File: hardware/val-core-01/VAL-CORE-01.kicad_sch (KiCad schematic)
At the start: 15 parts, among them J1 USB-C Device/UFP, J2 TRS MIDI OUT Type-A, J3 TRS MIDI IN Type-A, U1 ESP32-S3-MINI-1-N4R2, U2 TUSB320LAI, U3 3V3_REGULATOR_TBD_600mA, U4 SN74AHCT1G125, U5 MIDI_IN_OPTO_TBD

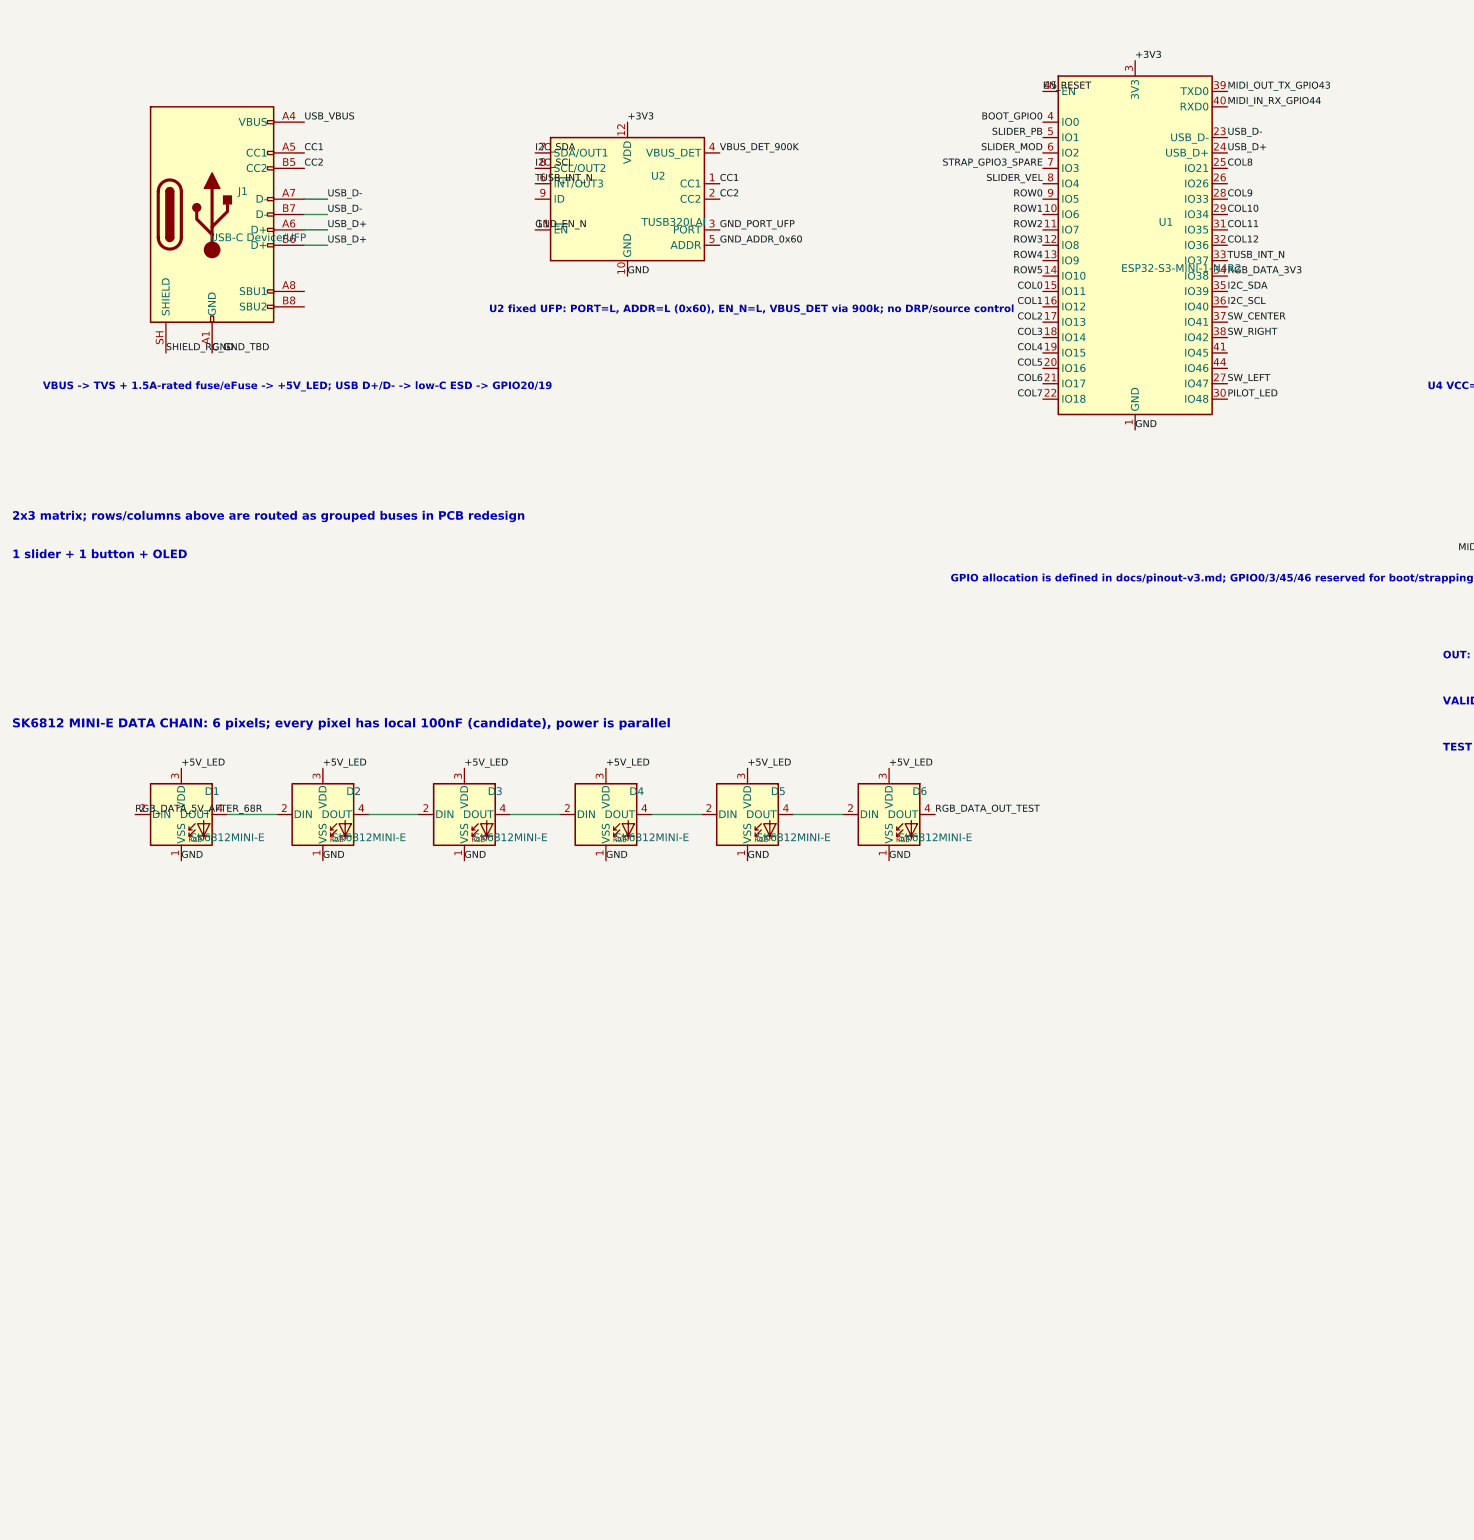
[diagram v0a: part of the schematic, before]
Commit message: VAL-CORE-01の旧CC回路と検証条件を現行仕様へ修正
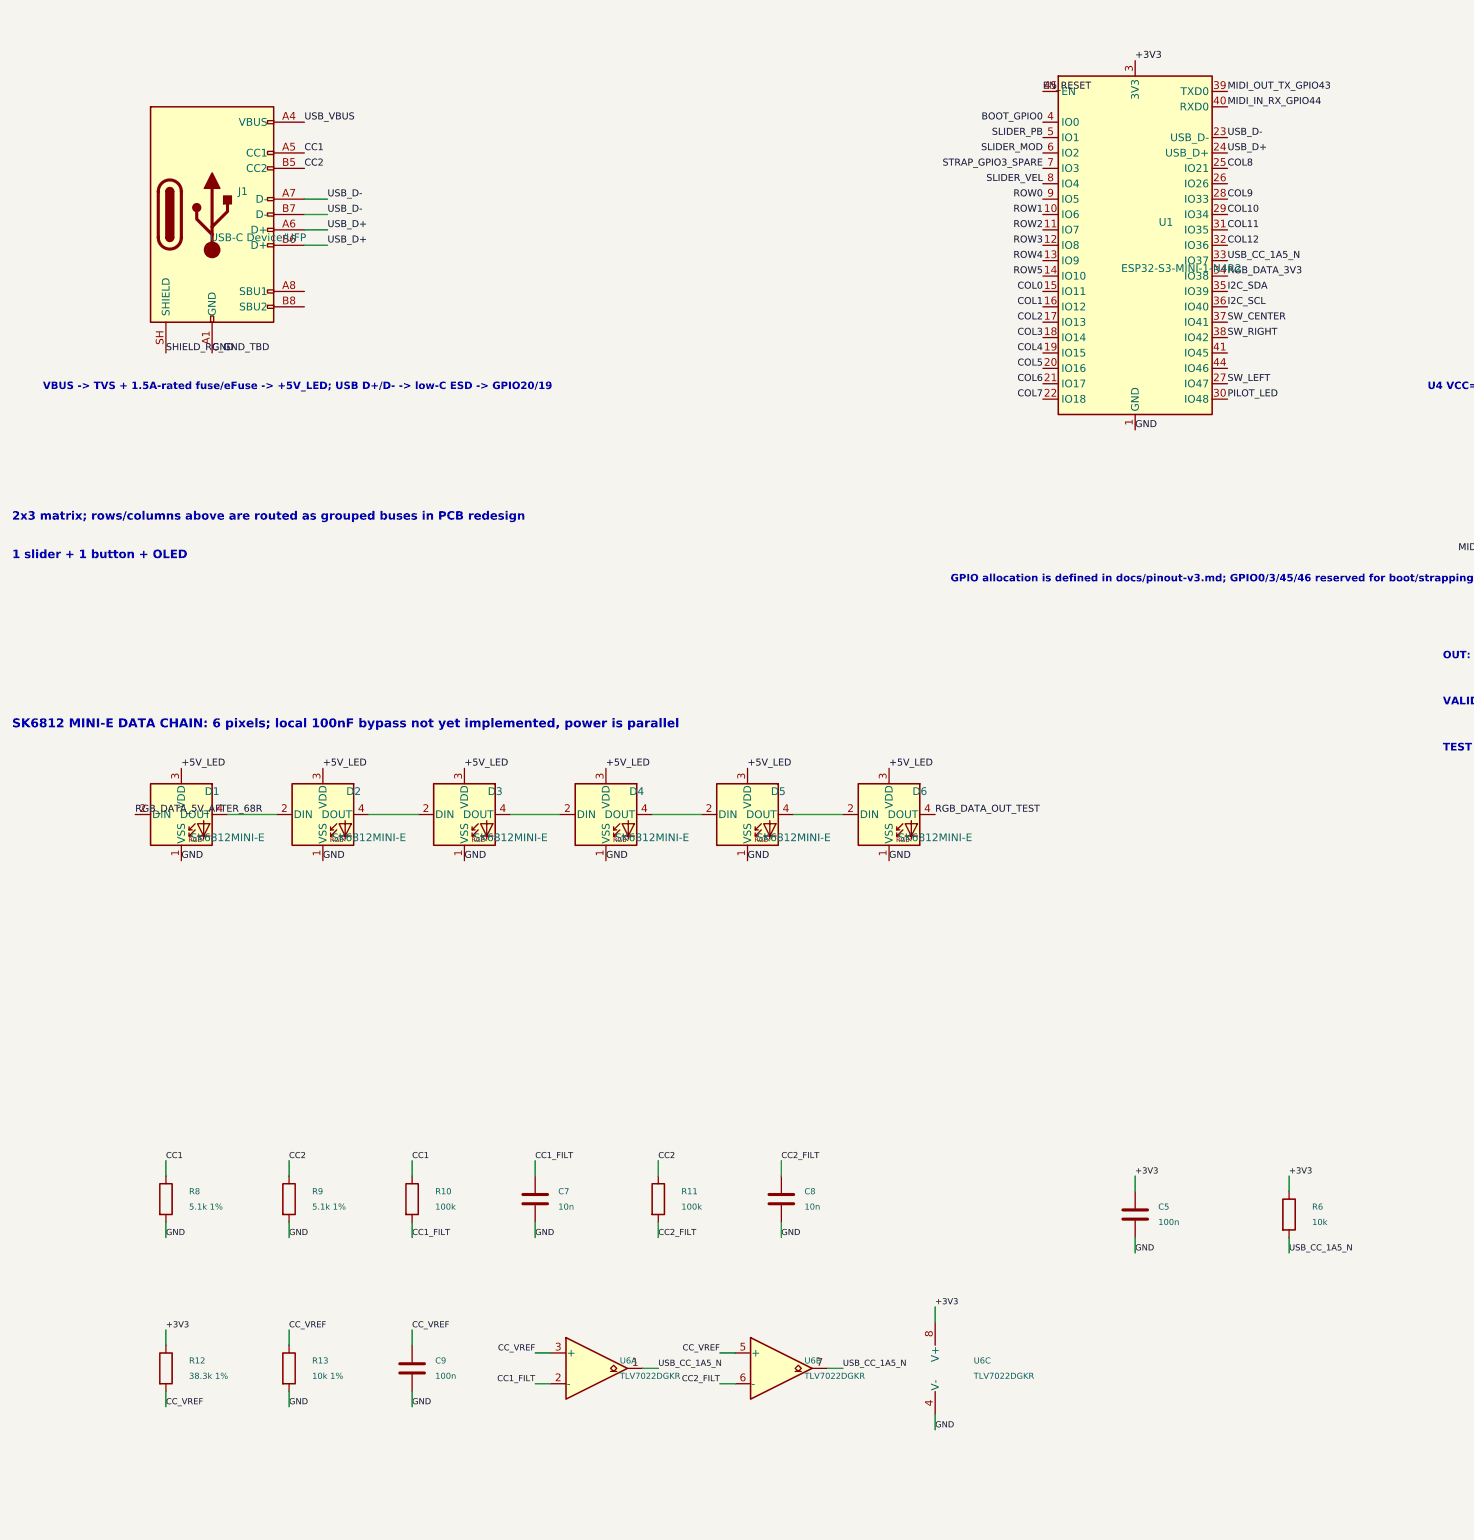
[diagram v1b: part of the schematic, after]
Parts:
- removed U2: TUSB320LAI, symbol Interface_USB:TUSB320
- added C5, C9: 100n, Capacitor_SMD:C_0603_1608Metric, symbol Device:C
- added C7, C8: 10n, Capacitor_SMD:C_0603_1608Metric, symbol Device:C
- added R10, R11: 100k, Resistor_SMD:R_0603_1608Metric, symbol Device:R
- added R12: 38.3k 1%, Resistor_SMD:R_0603_1608Metric, symbol Device:R
- added R13: 10k 1%, Resistor_SMD:R_0603_1608Metric, symbol Device:R
- added R6: 10k, Resistor_SMD:R_0603_1608Metric, symbol Device:R
- added R8, R9: 5.1k 1%, Resistor_SMD:R_0603_1608Metric, symbol Device:R
- added U6: TLV7022DGKR, Package_SO:VSSOP-8_3x3mm_P0.65mm, symbol Comparator:LM2903
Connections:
- net +3V3: now also C5.1, R12.1, R6.1, U6.8 (V+)
- net CC1: now also R10.1, R8.1
- net CC2: now also R11.1, R9.1
- net GND: now also C5.2, C7.2, C8.2, C9.2, R13.2, R8.2, R9.2, U6.4 (V-)
- net TUSB_INT_N renamed USB_CC_1A5_N
- net USB_CC_1A5_N: now also R6.2, U6.1, U6.7
- new net CC1_FILT: C7.1, R10.2, U6.2 (-)
- new net CC2_FILT: C8.1, R11.2, U6.6 (-)
- new net CC_VREF: C9.1, R12.2, R13.1, U6.3 (+), U6.5 (+)
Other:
- note added: "SK6812 MINI-E DATA CHAIN: 6 pixels; local 100nF bypass not yet implemented, power is parallel"
- note removed: "SK6812 MINI-E DATA CHAIN: 6 pixels; every pixel has local 100nF (candidate), power is parallel"
- note removed: "U2 fixed UFP: PORT=L, ADDR=L (0x60), EN_N=L, VBUS_DET via 900k; no DRP/source control"
